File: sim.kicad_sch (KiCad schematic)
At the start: 31 parts, among them J4 USB_B_Micro, J5 Conn_Coaxial, J6 SIM_Card, Q1 Q_NPN_BCE, U2 SIM800C

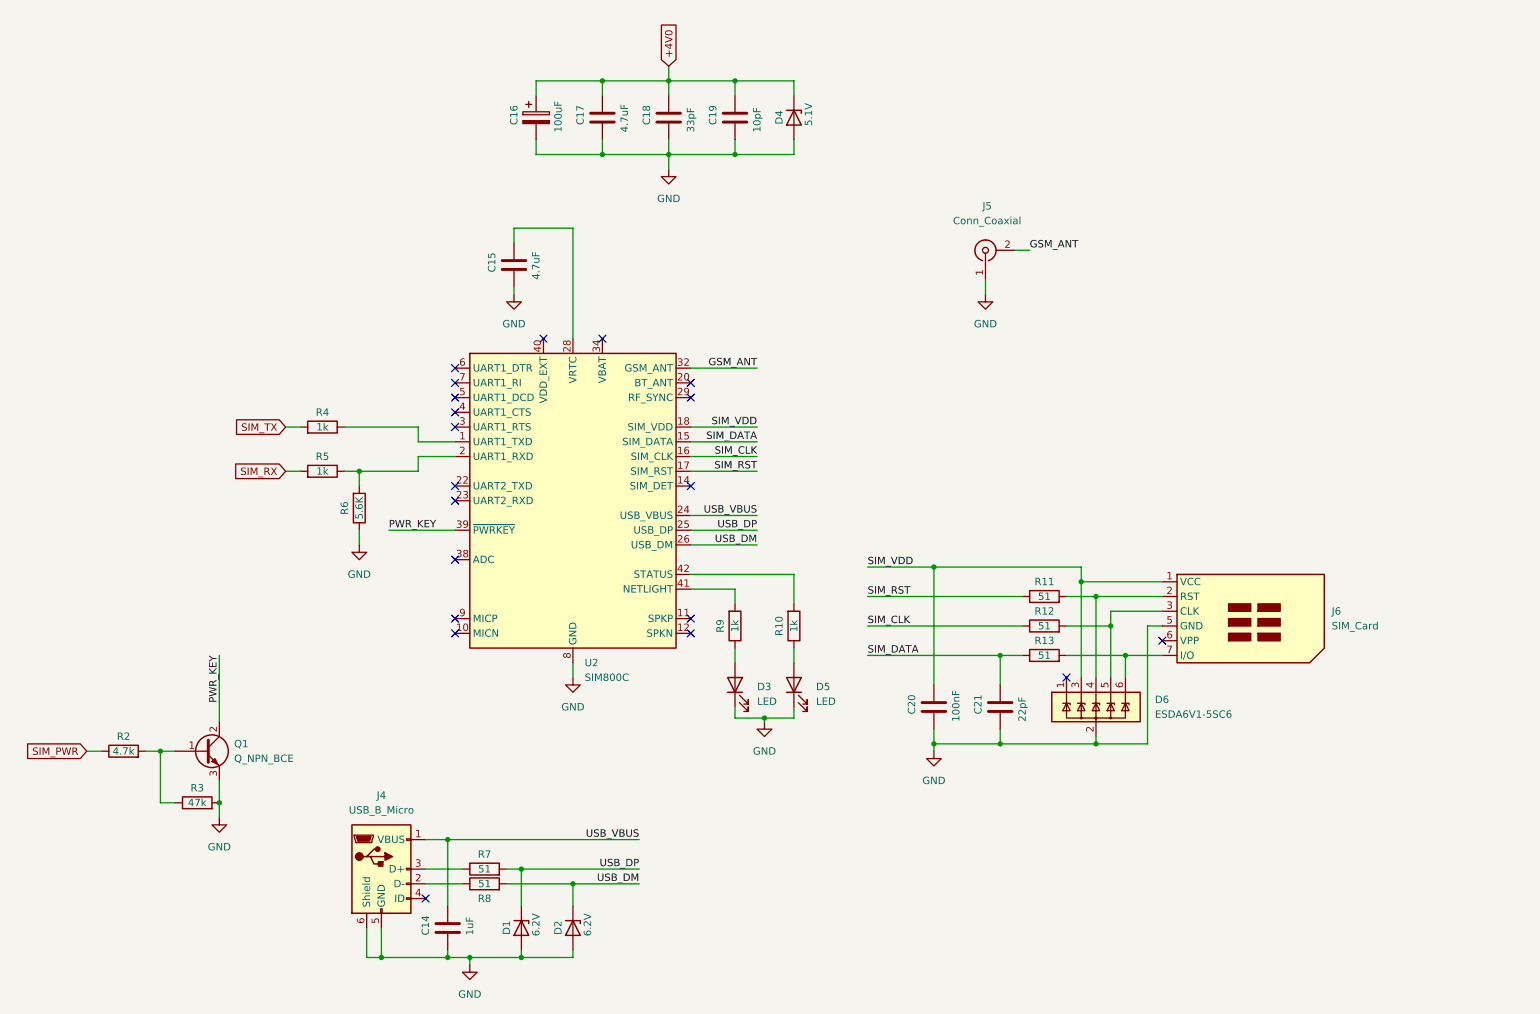
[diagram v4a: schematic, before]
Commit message: Assign footprints, change few elements in scheme
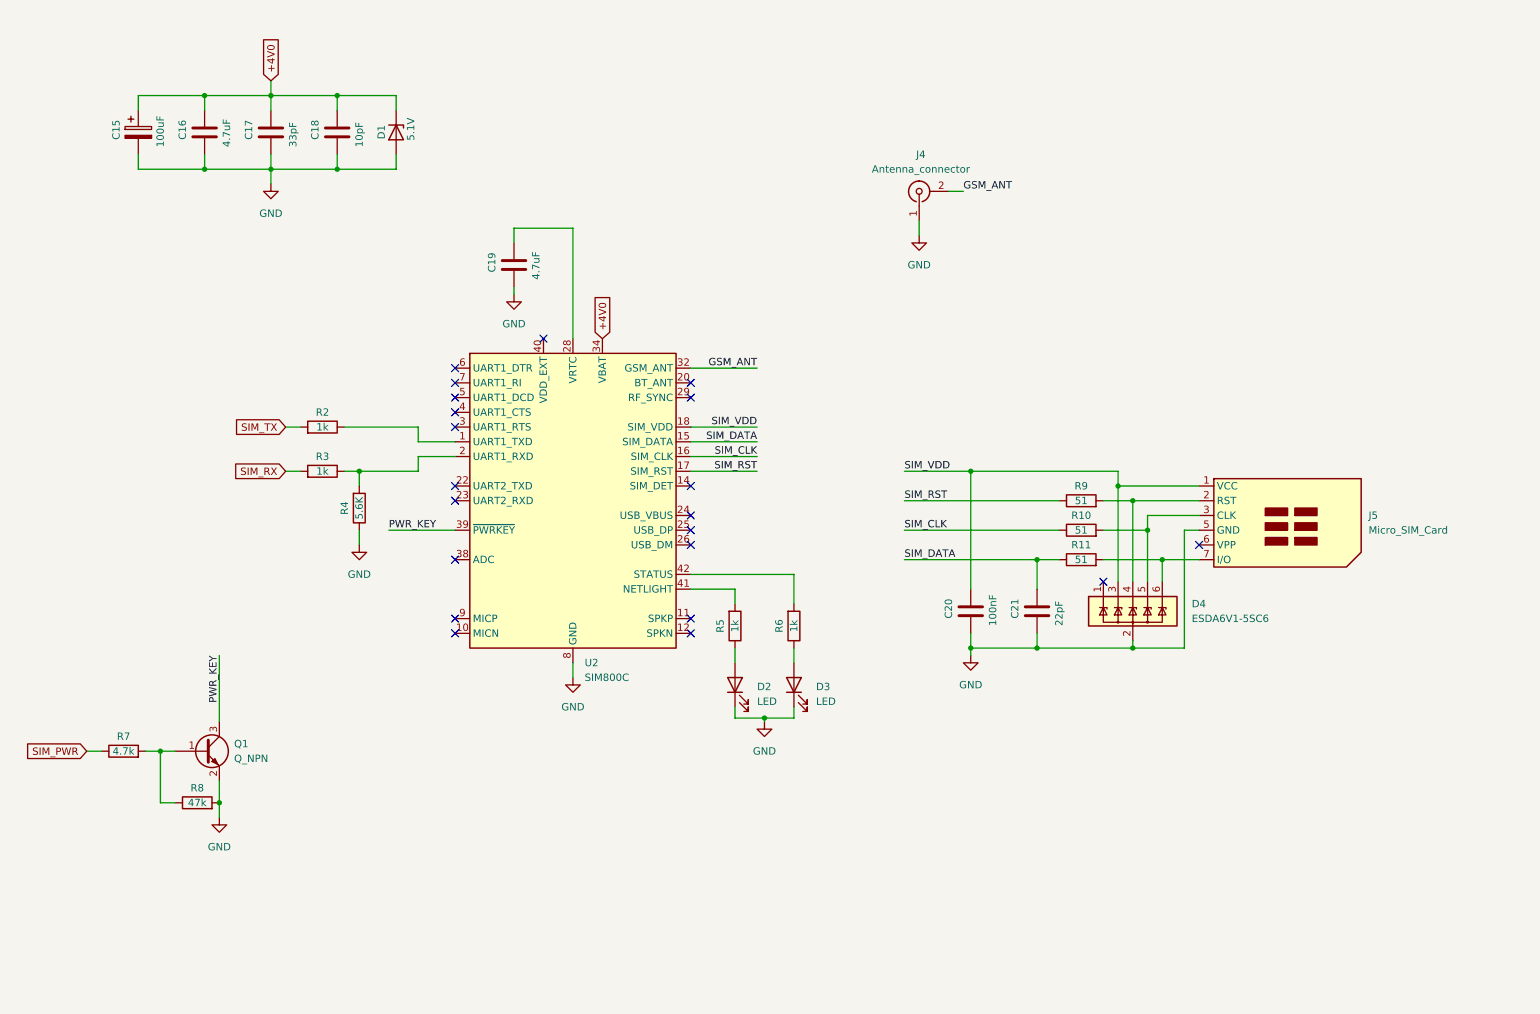
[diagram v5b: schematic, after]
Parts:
- removed C14: 1uF, symbol Device:C
- removed D1, D2: 6.2V, symbol Device:D_Zener
- removed J4: USB_B_Micro, symbol Connector:USB_B_Micro
- removed Q1: Q_NPN_BCE, symbol Device:Q_NPN_BCE
- removed R7, R8: 51, symbol Device:R
- added Q1: Q_NPN, Package_TO_SOT_SMD:SOT-23_Handsoldering, symbol Device:Q_NPN_BEC
- C15: renamed from C16; footprint (none) -> Capacitor_SMD:CP_Elec_5x5.4
- C16: renamed from C17; footprint (none) -> Capacitor_SMD:C_0603_1608Metric_Pad1.08x0.95mm_HandSolder
- C17: renamed from C18; footprint (none) -> Capacitor_SMD:C_0603_1608Metric_Pad1.08x0.95mm_HandSolder
- C18: renamed from C19; footprint (none) -> Capacitor_SMD:C_0603_1608Metric_Pad1.08x0.95mm_HandSolder
- C19: renamed from C15; footprint (none) -> Capacitor_SMD:C_0603_1608Metric_Pad1.08x0.95mm_HandSolder
- C20, C21: footprint (none) -> Capacitor_SMD:C_0603_1608Metric_Pad1.08x0.95mm_HandSolder
- D1: renamed from D4; footprint (none) -> Diode_SMD:D_SOD-323_HandSoldering
- D2: renamed from D3; footprint (none) -> LED_SMD:LED_0603_1608Metric
- D3: renamed from D5; footprint (none) -> LED_SMD:LED_0603_1608Metric
- J4: renamed from J5; value Conn_Coaxial -> Antenna_connector
- J5: renamed from J6; value SIM_Card -> Micro_SIM_Card; footprint (none) -> Connector_Card:microSIM_JAE_SF53S006VCBR2000
- R10: renamed from R12; footprint (none) -> Resistor_SMD:R_0603_1608Metric_Pad0.98x0.95mm_HandSolder
- R11: renamed from R13; footprint (none) -> Resistor_SMD:R_0603_1608Metric_Pad0.98x0.95mm_HandSolder
- R2: renamed from R4; footprint (none) -> Resistor_SMD:R_0603_1608Metric_Pad0.98x0.95mm_HandSolder
- R3: renamed from R5; footprint (none) -> Resistor_SMD:R_0603_1608Metric_Pad0.98x0.95mm_HandSolder
- R4: renamed from R6; footprint (none) -> Resistor_SMD:R_0603_1608Metric_Pad0.98x0.95mm_HandSolder
- R5: renamed from R9; footprint (none) -> Resistor_SMD:R_0603_1608Metric_Pad0.98x0.95mm_HandSolder
- R6: renamed from R10; footprint (none) -> Resistor_SMD:R_0603_1608Metric_Pad0.98x0.95mm_HandSolder
- R7: renamed from R2; footprint (none) -> Resistor_SMD:R_0603_1608Metric_Pad0.98x0.95mm_HandSolder
- R8: renamed from R3; footprint (none) -> Resistor_SMD:R_0603_1608Metric_Pad0.98x0.95mm_HandSolder
- R9: renamed from R11; footprint (none) -> Resistor_SMD:R_0603_1608Metric_Pad0.98x0.95mm_HandSolder
- renumbered D6 to D4
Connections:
- net +4V0: now also U2.34 (VBAT), U2.35 (VBAT)
- net GND: now also Q1.2 (E)
- net PWR_KEY: now also Q1.3 (C)
- net at R7.2, R8.1: now also Q1.1 (B)
- net USB_DM: no longer names the net of U2.26 (USB_DM)
- net USB_DP: no longer names the net of U2.25 (USB_DP)
- net USB_VBUS: no longer names the net of U2.24 (USB_VBUS)
- no-connect marks 20 -> 21
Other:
- moved on the sheet: C15, C16, C17, C18, C20, C21, D1, D4, J4, J5, R10, R11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

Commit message: Create bill of materials
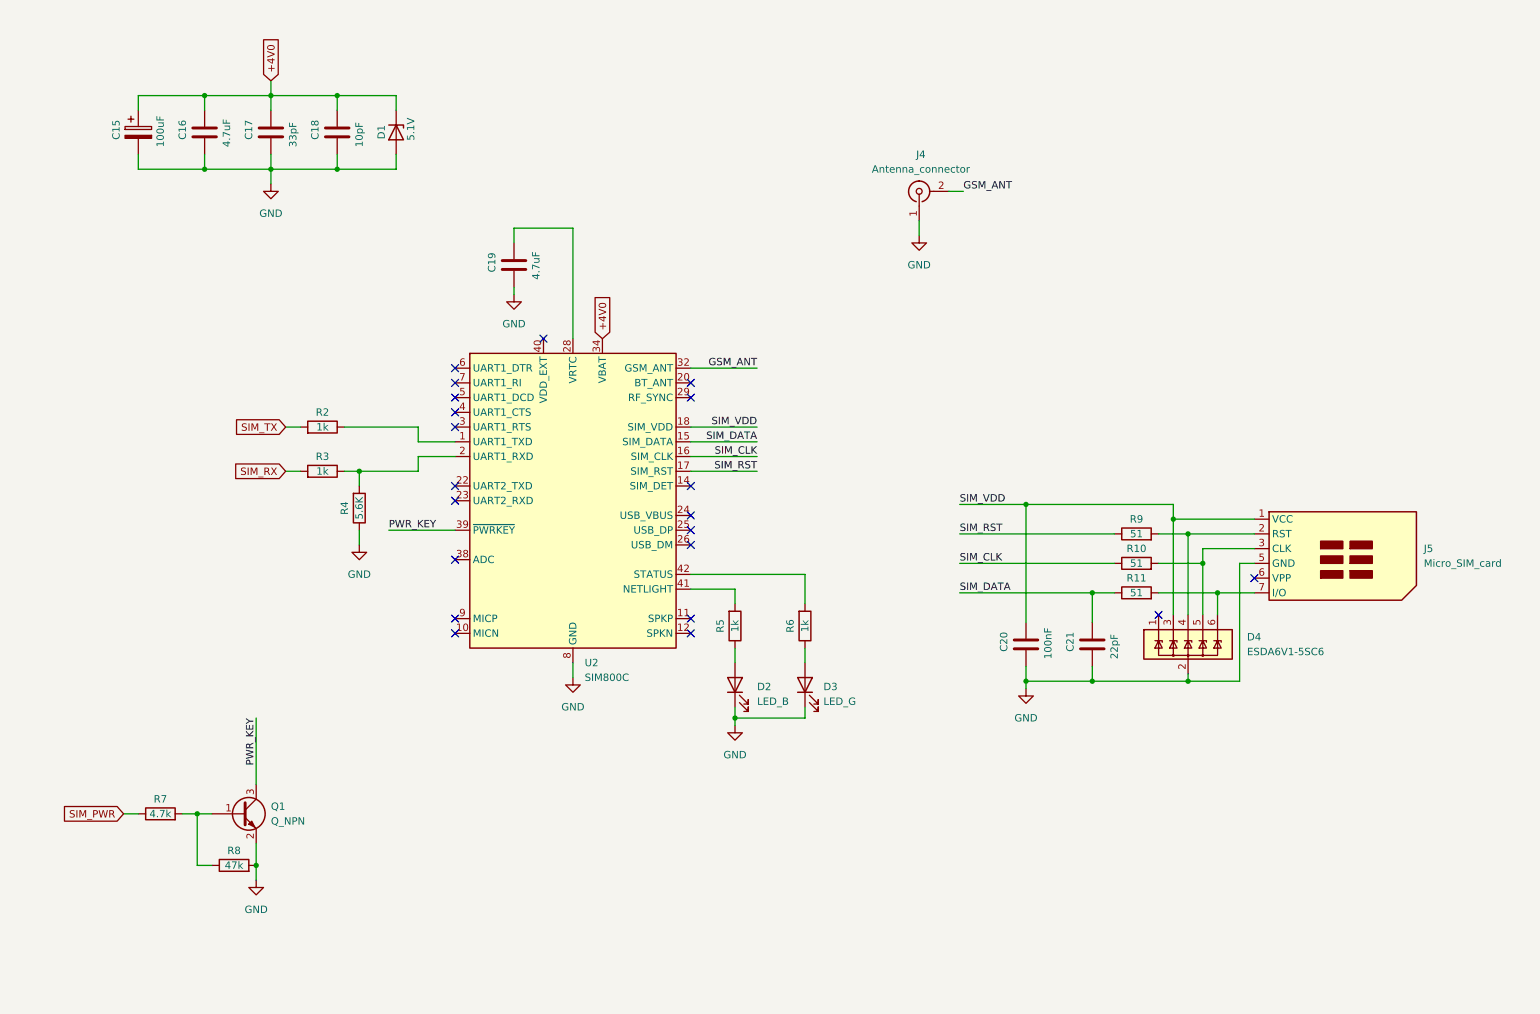
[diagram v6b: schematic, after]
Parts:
- D2: value LED -> LED_B
- D3: value LED -> LED_G
- J5: value Micro_SIM_Card -> Micro_SIM_card
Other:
- moved on the sheet: C20, C21, D3, D4, J5, Q1, R10, R11, R6, R7, R8, R9

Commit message: Add sub-schemes hierarchical labels
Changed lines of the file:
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@@
+    (stroke (width 0) (type default))
+  )
+  (wire (pts (xy 124.46 74.295) (xy 124.46 74.93))
     (stroke (width 0) (type default))
   )
@@
     (effects (font (size 1.27 1.27)) (justify left bottom))
   )
-  (global_label "SIM_TX" (shape input) (at 69.85 90.17 180) (fields_autoplaced)
+  (hierarchical_label "+4V0" (shape input) (at 67.31 30.48 90) (fields_autoplaced)
+    (effects (font (size 1.27 1.27)) (justify left))
+  )
+  (hierarchical_label "SIM_TX" (shape output) (at 69.85 90.17 180) (fields_autoplaced)
     (effects (font (size 1.27 1.27)) (justify right))
-    (property "Intersheetrefs" "${INTERSHEET_REFS}" (at 61.0264 90.0906 0)
-      (effects (font (size 1.27 1.27)) (justify right) hide)
-    )
   )
-  (global_label "SIM_RX" (shape input) (at 69.85 97.79 180) (fields_autoplaced)
+  (hierarchical_label "SIM_PWR" (shape input) (at 41.91 156.845 180) (fields_autoplaced)
     (effects (font (size 1.27 1.27)) (justify right))
-    (property "Intersheetrefs" "${INTERSHEET_REFS}" (at 60.724 97.7106 0)
-      (effects (font (size 1.27 1.27)) (justify right) hide)
-    )
   )
-  (global_label "SIM_PWR" (shape input) (at 41.91 156.845 180) (fields_autoplaced)
+  (hierarchical_label "SIM_RX" (shape input) (at 69.85 97.79 180) (fields_autoplaced)
     (effects (font (size 1.27 1.27)) (justify right))
-    (property "Intersheetrefs" "${INTERSHEET_REFS}" (at 31.2721 156.7656 0)
-      (effects (font (size 1.27 1.27)) (justify right) hide)
-    )
   )
-  (global_label "+4V0" (shape input) (at 67.31 30.48 90) (fields_autoplaced)
+  (hierarchical_label "+4V0" (shape input) (at 124.46 74.295 90) (fields_autoplaced)
     (effects (font (size 1.27 1.27)) (justify left))
-    (property "Intersheetrefs" "${INTERSHEET_REFS}" (at 67.31 22.4148 90)
-      (effects (font (size 1.27 1.27)) (justify left) hide)
-    )
-  )
-  (global_label "+4V0" (shape input) (at 124.46 74.93 90) (fields_autoplaced)
-    (effects (font (size 1.27 1.27)) (justify left))
-    (property "Intersheetrefs" "${INTERSHEET_REFS}" (at 124.46 66.8648 90)
-      (effects (font (size 1.27 1.27)) (justify left) hide)
-    )
   )
   (symbol (lib_id "Device:C") (at 109.22 62.23 0) (unit 1)

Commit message: Assign antenna, camera and crystal footprint
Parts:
- J4: footprint (none) -> Connector_Coaxial:U.FL_Molex_MCRF_73412-0110_Vertical
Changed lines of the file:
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@@
       (effects (font (size 1.27 1.27)))
     )
-    (property "Footprint" "" (at 179.07 49.53 0)
+    (property "Footprint" "Connector_Coaxial:U.FL_Molex_MCRF_73412-0110_Vertical" (at 179.07 49.53 0)
       (effects (font (size 1.27 1.27)) hide)
     )
